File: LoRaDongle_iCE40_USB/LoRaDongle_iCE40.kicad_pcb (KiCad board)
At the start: 4 copper layers, 110 x 45 mm, 129 parts, among them IC1 93LC56BT-I_OT, IC2 ICE40UP5K-UWG30ITR1K, IC3 N25Q032A13ESC40F, J1 USB_A, J2 Conn_01x08, J3 Conn_02x02_Top_Bottom, J4 Jumper, J5 142-0701-801, J6 Conn_01x06, J7 Jumper_NC_Small, J8 Jumper, J9 Conn_02x02_Top_Bottom, SW1 SW_Push, U1 RP550K0001A-TR, U2 FT232H, U3 SX1261IMLTRT, U4 SKY13587-378LF, X1 ECS-2520MV-500-BL-TR, Y1 Crystal_GND24_Small, Y2 Crystal_GND24

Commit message: updating unconnected traces
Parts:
- moved R1 0.50 mm to (110.5, 97.0)
- moved R2 0.50 mm to (110.5, 98.0)
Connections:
- net /USB_Interface/UBS_D+ renamed /USB_Interface/USB_D+
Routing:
- net Net-(R11-Pad1): track 0.00 -> 10.7 mm, vias 0 -> 2
- net GND: track 187.2 -> 192.1 mm, vias 75 -> 76
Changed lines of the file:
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@@
   (net 91 "/D-")
   (net 92 "/D+")
-  (net 93 "/USB_Interface/UBS_D+")
+  (net 93 "/USB_Interface/USB_D+")
   (net 94 "/USB_Interface/USB_D-")
   (net 95 "RadioPower")
@@
   )
   (footprint "Resistor_SMD:R_0402_1005Metric_Pad0.72x0.64mm_HandSolder" (layer "F.Cu")
-    (at 110.5 98.5 180)
+    (at 110.5 98 180)
     (descr "Resistor SMD 0402 (1005 Metric), square (rectangular) end terminal, IPC_7351 nominal with elongated pad for handsoldering. (Body size source: IPC-SM-782 page 72, https://www.pcb-3d.com/wordpress/wp-content/uploads/ipc-sm-782a_amendment_1_and_2.pdf), generated with kicad-footprint-generator")
     (tags "resistor handsolder")
@@
   )
   (footprint "Resistor_SMD:R_0402_1005Metric_Pad0.72x0.64mm_HandSolder" (layer "F.Cu")
-    (at 110.5 96.5 180)
+    (at 110.5 97 180)
     (descr "Resistor SMD 0402 (1005 Metric), square (rectangular) end terminal, IPC_7351 nominal with elongated pad for handsoldering. (Body size source: IPC-SM-782 page 72, https://www.pcb-3d.com/wordpress/wp-content/uploads/ipc-sm-782a_amendment_1_and_2.pdf), generated with kicad-footprint-generator")
     (tags "resistor handsolder")
@@
     (fp_line (start 0.525 -0.27) (end 0.525 0.27) (layer "F.Fab") (width 0.1))
     (pad "1" smd roundrect locked (at -0.5975 0 180) (size 0.715 0.64) (layers "F.Cu" "F.Paste" "F.Mask") (roundrect_rratio 0.25)
-      (net 93 "/USB_Interface/UBS_D+") (pintype "passive"))
+      (net 93 "/USB_Interface/USB_D+") (pintype "passive"))
     (pad "2" smd roundrect locked (at 0.5975 0 180) (size 0.715 0.64) (layers "F.Cu" "F.Paste" "F.Mask") (roundrect_rratio 0.25)
       (net 92 "/D+") (pintype "passive"))
@@
       (net 94 "/USB_Interface/USB_D-") (pinfunction "DM") (pintype "bidirectional"))
     (pad "7" smd roundrect locked (at -4.1625 0.25) (size 1.475 0.3) (layers "F.Cu" "F.Paste" "F.Mask") (roundrect_rratio 0.25)
-      (net 93 "/USB_Interface/UBS_D+") (pinfunction "DP") (pintype "bidirectional"))
+      (net 93 "/USB_Interface/USB_D+") (pinfunction "DP") (pintype "bidirectional"))
     (pad "8" smd roundrect locked (at -4.1625 0.75) (size 1.475 0.3) (layers "F.Cu" "F.Paste" "F.Mask") (roundrect_rratio 0.25)
       (net 10 "/USB_Interface/VPLL") (pinfunction "VPLL") (pintype "power_in"))
@@
   (segment (start 121.0685 101.9885) (end 121.0685 101.9885) (width 0.3) (layer "F.Cu") (net 1))
   (segment (start 120.0475 99.3175) (end 120.0475 99.3175) (width 0.3) (layer "F.Cu") (net 1))
-  (segment (start 114.92 98.2) (end 114.92 98.2) (width 0.3) (layer "F.Cu") (net 1))
   (segment (start 179.93 110.47) (end 182.34 110.47) (width 1) (layer "F.Cu") (net 1))
   (segment (start 121.6375 93.1) (end 121.6375 94.3375) (width 0.4) (layer "F.Cu") (net 1))
@@
   (segment (start 135.25 101.6625) (end 135.25 103.91) (width 0.3) (layer "F.Cu") (net 1))
   (segment (start 173.37 95.99) (end 173.37 95.47) (width 0.3) (layer "F.Cu") (net 1))
+  (segment (start 105.65 94) (end 107.83 94) (width 0.5) (layer "F.Cu") (net 1))
   (segment (start 119.15 99.3175) (end 120.0475 99.3175) (width 0.3) (layer "F.Cu") (net 1))
   (segment (start 178.96 107.09) (end 178.96 109.5) (width 1) (layer "F.Cu") (net 1))
@@
   (segment (start 131.25 92.6175) (end 130.66625 92.03375) (width 0.3) (layer "F.Cu") (net 1))
   (segment (start 182.61 94.9025) (end 182.61 93.87) (width 0.3) (layer "F.Cu") (net 1))
+  (segment (start 107.83 94) (end 109.26 92.57) (width 0.5) (layer "F.Cu") (net 1))
   (segment (start 173.37 95.99) (end 173.37 97.24) (width 0.3) (layer "F.Cu") (net 1))
   (segment (start 188.75 82.72) (end 186.1 82.72) (width 1) (layer "F.Cu") (net 1))
@@
   (segment (start 186.1 82.72) (end 183.14 82.72) (width 1) (layer "F.Cu") (net 1))
   (segment (start 202.93 110.47) (end 205.35 110.47) (width 1) (layer "F.Cu") (net 1))
+  (segment (start 114.92 98.2) (end 114.49 98.63) (width 0.3) (layer "F.Cu") (net 1))
   (segment (start 200.31 110.47) (end 202.93 110.47) (width 1) (layer "F.Cu") (net 1))
   (segment (start 198.82 97.7575) (end 198.82 98.92) (width 0.3) (layer "F.Cu") (net 1))
@@
   (via micro (at 155.67 98.09) (size 0.3) (drill 0.15) (layers "F.Cu" "In1.Cu") (net 1))
   (via (at 208.87 103.25) (size 1) (drill 0.5) (layers "F.Cu" "B.Cu") (net 1))
+  (via (at 114.49 98.63) (size 0.8) (drill 0.4) (layers "F.Cu" "B.Cu") (net 1))
   (via (at 121.0685 101.9885) (size 0.8) (drill 0.4) (layers "F.Cu" "B.Cu") (net 1))
   (via (at 209.07 84.89) (size 1) (drill 0.5) (layers "F.Cu" "B.Cu") (net 1))
@@
   (via (at 182.34 110.47) (size 1) (drill 0.5) (layers "F.Cu" "B.Cu") (net 1))
   (via (at 169.4 95.81) (size 0.6) (drill 0.3) (layers "F.Cu" "B.Cu") (free) (net 1))
-  (via (at 114.92 98.2) (size 0.8) (drill 0.4) (layers "F.Cu" "B.Cu") (net 1))
   (via micro (at 175.05 94.88) (size 0.4) (drill 0.2) (layers "F.Cu" "In1.Cu") (net 1))
   (via (at 192.028 106.222) (size 0.8) (drill 0.4) (layers "F.Cu" "B.Cu") (net 1))
@@
   (via (at 125.58 100.38) (size 0.8) (drill 0.4) (layers "F.Cu" "B.Cu") (net 1))
   (via (at 196.96 82.72) (size 1) (drill 0.5) (layers "F.Cu" "B.Cu") (net 1))
+  (via (at 109.26 92.57) (size 1) (drill 0.5) (layers "F.Cu" "B.Cu") (net 1))
   (via (at 139.1575 103.0475) (size 0.8) (drill 0.4) (layers "F.Cu" "B.Cu") (net 1))
   (via (at 137.25 103.85) (size 0.8) (drill 0.4) (layers "F.Cu" "B.Cu") (net 1))
@@
   (segment (start 170.25 97) (end 168.055 97) (width 0.3) (layer "F.Cu") (net 72))
   (segment (start 168.055 97) (end 166.52 95.465) (width 0.3) (layer "F.Cu") (net 72))
+  (segment (start 128.02 96.65) (end 128.12 96.75) (width 0.3) (layer "F.Cu") (net 73))
+  (segment (start 122.788 101.092) (end 123.13 100.75) (width 0.3) (layer "F.Cu") (net 73))
+  (segment (start 129.3075 96.78) (end 129.3375 96.75) (width 0.15) (layer "F.Cu") (net 73))
+  (segment (start 122.2635 101.092) (end 122.788 101.092) (width 0.3) (layer "F.Cu") (net 73))
+  (segment (start 126.07 96.65) (end 128.02 96.65) (width 0.3) (layer "F.Cu") (net 73))
+  (segment (start 123.13 100.75) (end 123.13 99.64) (width 0.3) (layer "F.Cu") (net 73))
+  (segment (start 128.12 96.75) (end 129.3375 96.75) (width 0.3) (layer "F.Cu") (net 73))
+  (via (at 126.07 96.65) (size 0.8) (drill 0.4) (layers "F.Cu" "B.Cu") (net 73))
+  (via (at 123.13 99.64) (size 0.8) (drill 0.4) (layers "F.Cu" "B.Cu") (net 73))
+  (segment (start 124.39 96.65) (end 126.07 96.65) (width 0.3) (layer "B.Cu") (net 73))
+  (segment (start 123.13 97.91) (end 124.39 96.65) (width 0.3) (layer "B.Cu") (net 73))
+  (segment (start 123.13 99.64) (end 123.13 97.91) (width 0.3) (layer "B.Cu") (net 73))
   (segment (start 190.728 106.228) (end 190.728 106.228) (width 0.3) (layer "F.Cu") (net 74))
   (segment (start 171.02 99.24) (end 170.97 99.19) (width 0.15) (layer "F.Cu") (net 74))
@@
   (segment (start 173.125 93.875) (end 173.125 91.7) (width 0.3) (layer "F.Cu") (net 88))
   (segment (start 173.87 95.99) (end 173.87 94.62) (width 0.3) (layer "F.Cu") (net 88))
+  (segment (start 109.627501 97.725001) (end 109.9025 98) (width 0.2) (layer "F.Cu") (net 91))
+  (segment (start 129.2975 97.29) (end 129.3375 97.25) (width 0.2) (layer "F.Cu") (net 94))
   (segment (start 167.2775 98.3225) (end 167.2775 98.3225) (width 0.4) (layer "F.Cu") (net 95))
   (segment (start 169.6 98.3225) (end 169.62 98.3025) (width 0.4) (layer "F.Cu") (net 95))

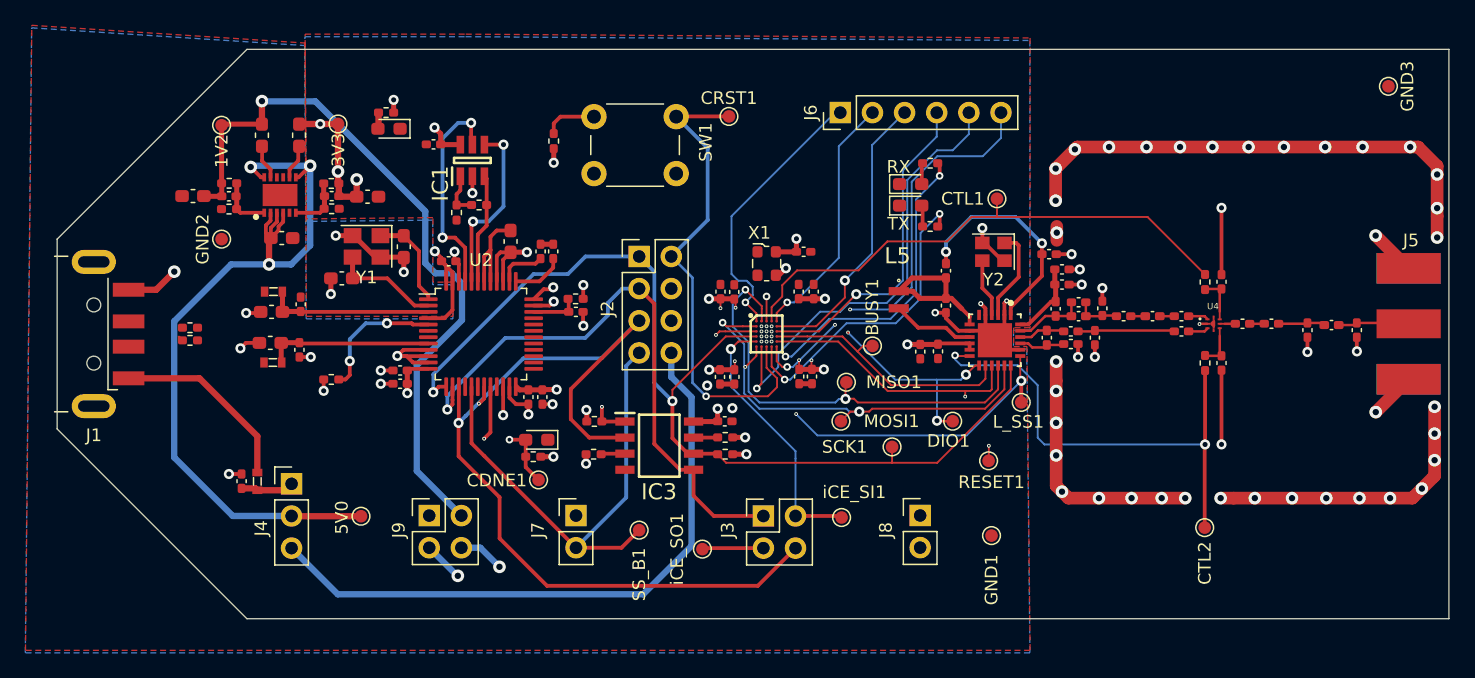
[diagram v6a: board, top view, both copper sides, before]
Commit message: updating symbol details
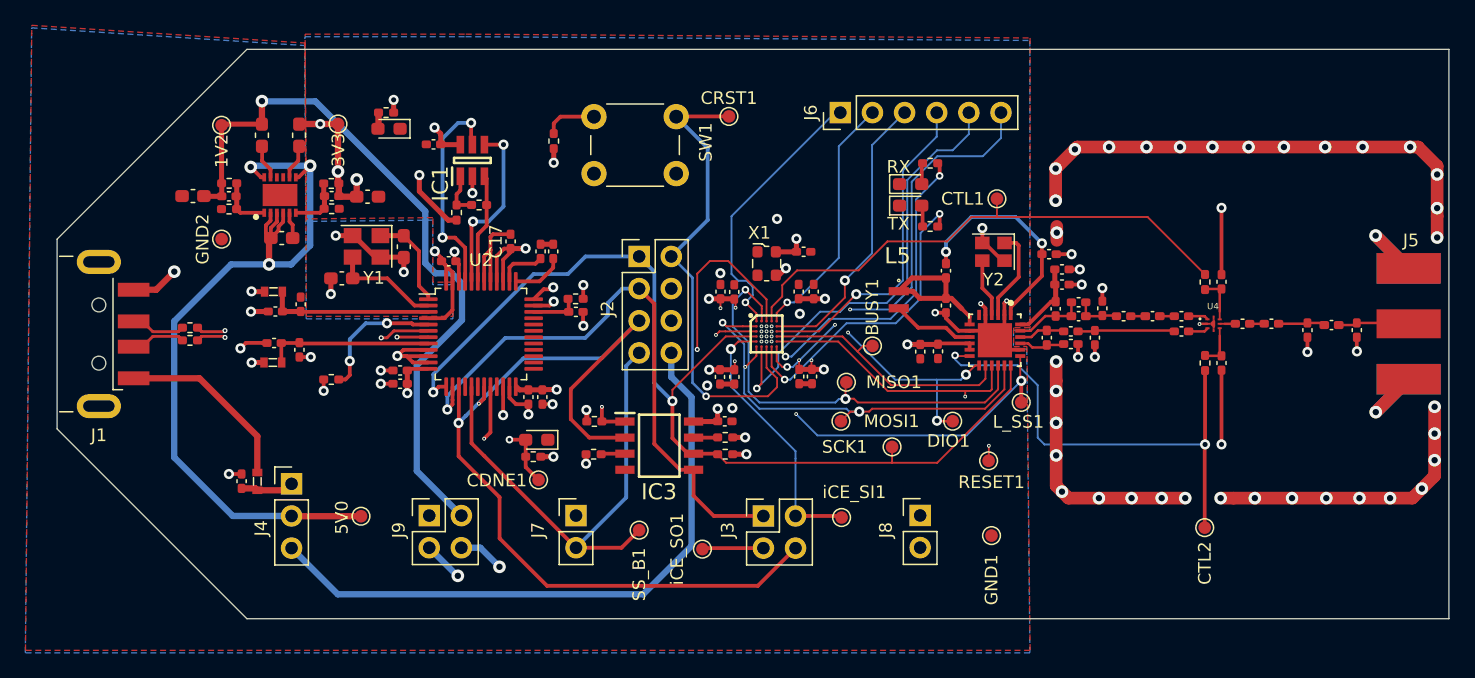
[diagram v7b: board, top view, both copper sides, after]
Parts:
- removed GND3: GND, TestPoint:TestPoint_Pad_D1.0mm
- C11, C17, C7: footprint Capacitor_SMD:C_0603_1608Metric_Pad1.08x0.95mm_HandSolder -> Capacitor_SMD:C_0402_1005Metric_Pad0.74x0.62mm_HandSolder
- moved J1 0.40 mm to (96.4, 97.5)
- moved C7 0.30 mm to (117.2, 95.7)
- moved C11 0.30 mm to (117.2, 98.2)
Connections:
- C41 pad 2: /RF Circuitry/VCTL1 -> /RF Circuitry/CTL1
- C43 pad 1: /RF Circuitry/VCTL2 -> /RF Circuitry/CTL2
- R18 pad 1: /RF Circuitry/VCTL1 -> /RF Circuitry/CTL1
- R19 pad 2: /RF Circuitry/VCTL2 -> /RF Circuitry/CTL2
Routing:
- net /USB_Interface/USB_D-: track 0.06 -> 18.8 mm, vias 0 -> 2
- net /USB_Interface/USB_D+: track 0.00 -> 18.6 mm, vias 0 -> 2
- net 3V3FPGA: track 79.7 -> 95.9 mm
- net GND: track 192.1 -> 208.1 mm, vias 76 -> 79
- net 3V3: track 44.6 -> 52.1 mm, vias 18 -> 21
- net /D-: track 0.39 -> 4.71 mm
- net /D+: track 0.00 -> 4.32 mm
- net /RF Circuitry/VCTL1: track 3.78 -> 0.00 mm
- net /RF Circuitry/CTL1: track 0.00 -> 3.78 mm
- net /RF Circuitry/VCTL2: track 3.55 -> 0.00 mm
- net /RF Circuitry/CTL2: track 0.00 -> 3.55 mm

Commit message: updated BOM
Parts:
- D1: value LED -> PWR; footprint LED_SMD:LED_0603_1608Metric_Pad1.05x0.95mm_HandSolder -> LED_SMD:LED_0805_2012Metric_Pad1.15x1.40mm_HandSolder
- L4: value 15nH -> 18nH
- R20, R21, R3: value R -> 100R
- R4: value 450K -> 453K
- U1: value RP550K0001A-TR -> RP550K001A-TR
- moved D1 0.35 mm to (126.5, 81.5)
